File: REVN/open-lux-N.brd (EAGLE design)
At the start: 53 x 68.6 mm, 71 parts, among them IC2 MCP73831, IC3 ATMEGA32U4-AU, IC4 MCP1700-33, J2 EG1206, Q1 BSS123, Q4 BSS123, T1 FDN340P, T2 FDN340P, X2 USBSMD, X3 8MHz

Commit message: update
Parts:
- moved IC4 1.63 mm to (7.62, 38.1)
- moved J2 1.27 mm to (2.03, 31.8)
- moved B2 0.25 mm to (49.3, 55.1)
- moved B1 0.25 mm to (15.2, 64.8)
- renumbered CN1 to JST, R-BTN to RESET
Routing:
- net A0: track 128.6 -> 135.2 mm
- net N$1: track 13.6 -> 15.8 mm
- net GND: track 468.0 -> 469.9 mm
- net VCC: track 418.2 -> 419.9 mm
- net D5: track 84.6 -> 85.9 mm
- net RXD: track 40.0 -> 39.1 mm
- net VBAT: track 101.7 -> 102.7 mm
- net A2: track 82.4 -> 83.0 mm
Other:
- board text added: "***"
- board text added: "A0"
- board text added: "A1"
- board text added: "A2"
- board text added: "A3"
- board text added: "A4"
- board text added: "D8"
- board text added: "D9"
- board text added: "GND"
- board text added: "LCD"
- board text added: "LED"
- board text added: "LUXNIR"
- board text added: "MISO"
- board text added: "MOSI"
- board text added: "PUBLICLAB.ORG/WIKI/OPEN-LUX"
- board text added: "REV-N"
- board text added: "RGB"
- board text added: "RST"
- board text added: "RX"
- board text added: "SCK"
- board text added: "SCL"
- board text added: "SDA"
- board text added: "TX"
- board text added: "USB"
- board text added: "VBUS"
- board text added: "VCC"

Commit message: update
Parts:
- moved JST 0.25 mm to (3.56, 45.2)
- renumbered RESET to RST
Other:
- board text added: "** **"
- board text added: "*****"
- board text added: "CERN Open"
- board text added: "Hardware Licesne"
- board text added: "LAB"
- board text added: "PUBLIC"
- board text added: "Ver. 1.1"
- board text removed: "***"
- board text removed: "PUBLICLAB.ORG"

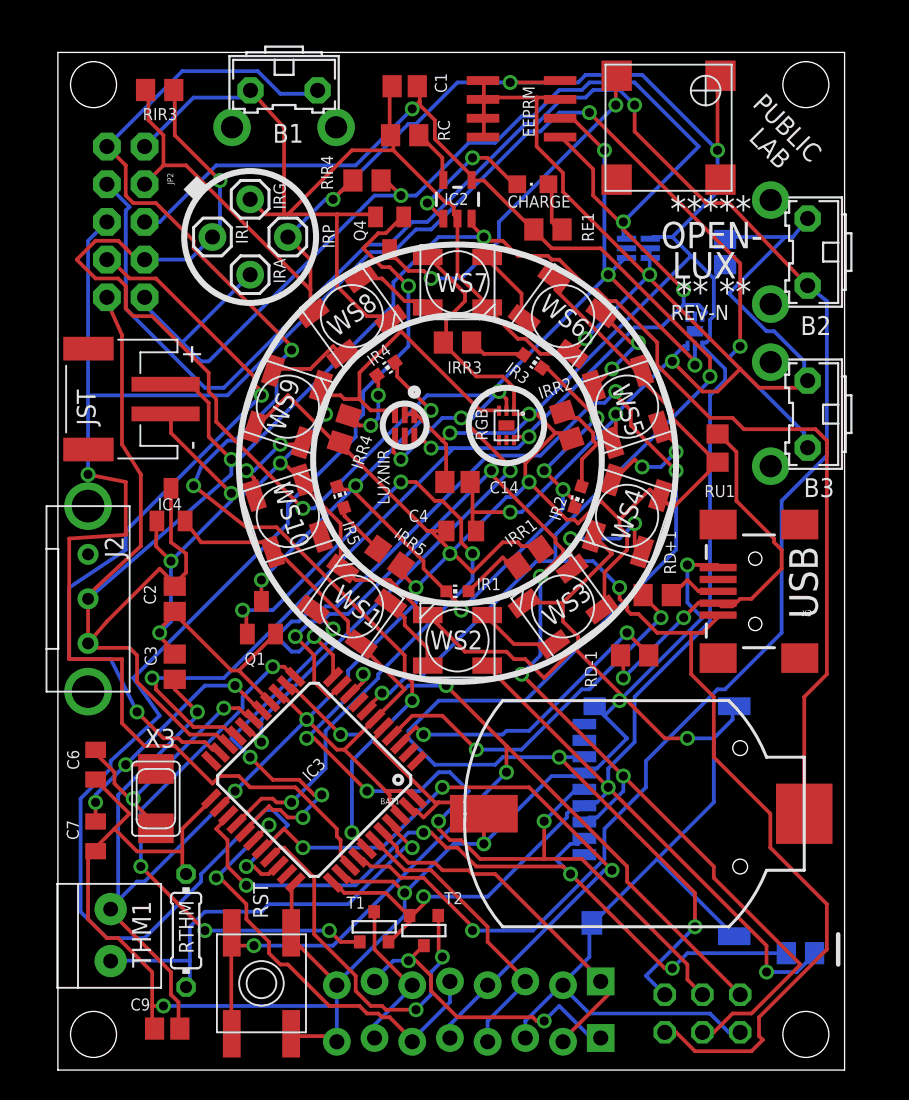
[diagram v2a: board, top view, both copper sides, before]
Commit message: fully routed, no DRC errors.
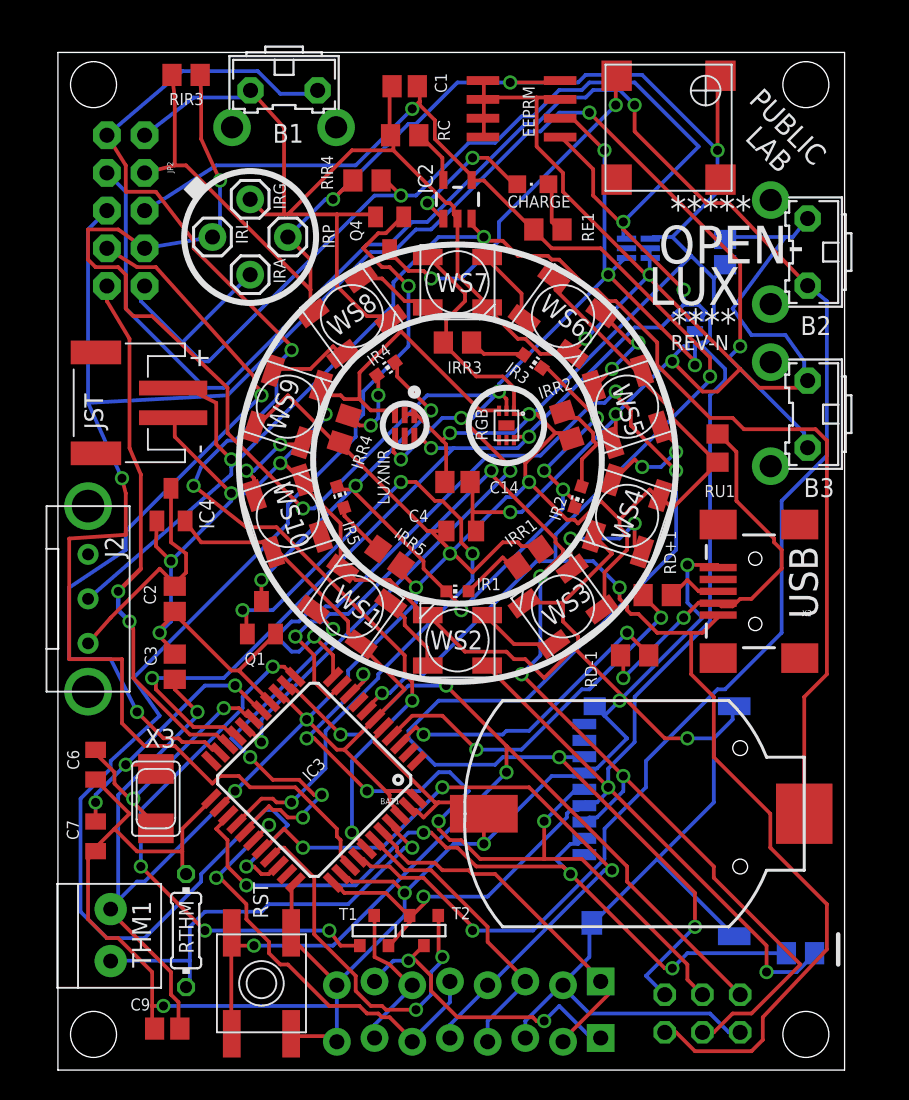
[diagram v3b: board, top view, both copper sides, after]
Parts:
- moved RIR3 2.05 mm to (8.64, 67.1)
- moved JP2 0.76 mm to (4.57, 57.9)
- moved JST 0.57 mm to (4.06, 45.0)
- moved T1 0.25 mm to (21.3, 9.40)
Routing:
- net RXD: track 39.0 -> 36.3 mm, vias 0 -> 2
- net VBUS: track 140.8 -> 139.8 mm
- net VBAT: track 102.8 -> 103.7 mm
- net GND: track 470.2 -> 469.4 mm
- net A0: track 135.2 -> 134.4 mm
- net SDA: track 141.1 -> 141.8 mm
- net A1: track 138.7 -> 139.3 mm
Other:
- board text added: "****"
- board text removed: "** **"
